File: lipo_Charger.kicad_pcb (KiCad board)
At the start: 4 copper layers, 99 parts, among them J1 XT60PW-M, J3 balance_plug_4s, J4 Conn_01x05, J5 Conn_01x04, J7 Conn_01x07, Q1 NX7002AK_215(nch low power), Q2 NVTFS010N10MCLTAG(high power), Q3 NVTFS010N10MCLTAG(high power), Q4 NVTFS010N10MCLTAG(high power), Q5 NVTFS010N10MCLTAG(high power)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

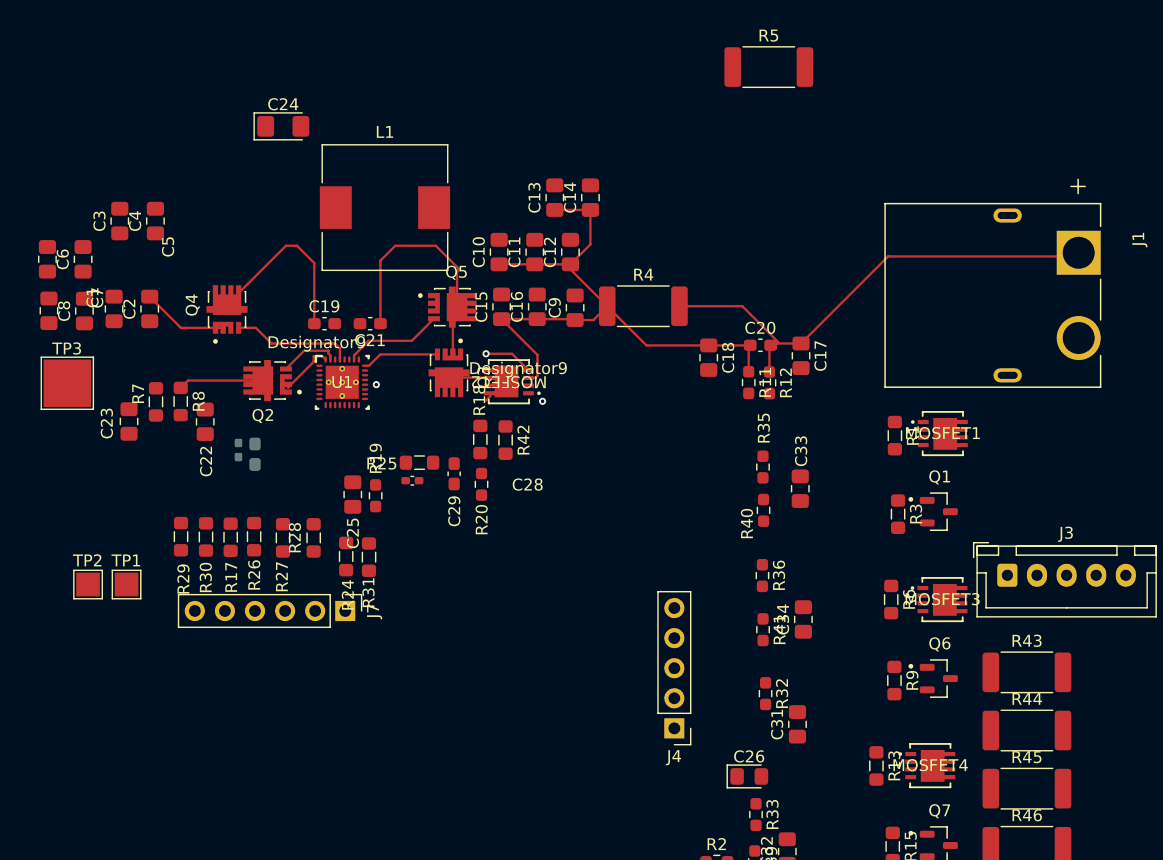
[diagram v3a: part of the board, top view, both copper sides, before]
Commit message: power side routing is done need to look into where i switch layers balancing side and interection with stm has to be done
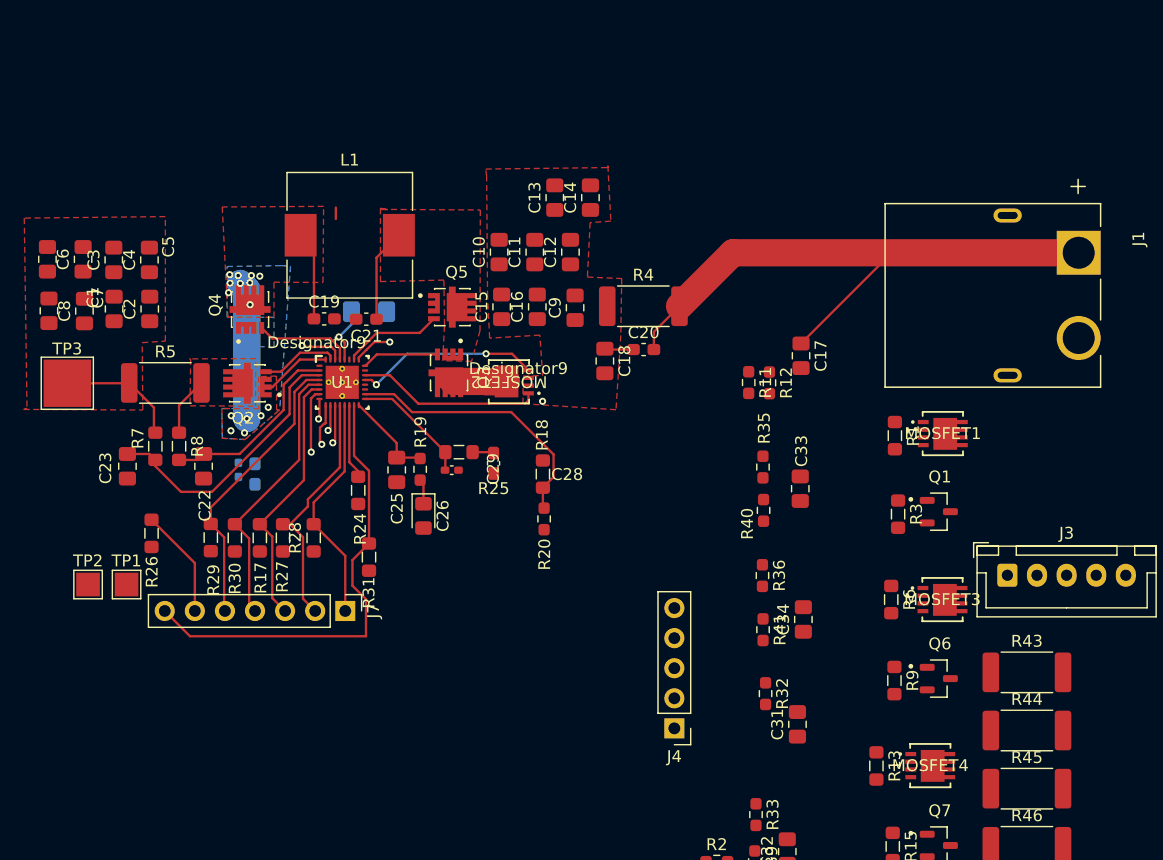
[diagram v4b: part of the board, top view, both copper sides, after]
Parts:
- removed R42: 10k, Inductor_SMD:L_0805_2012Metric_Pad1.05x1.20mm_HandSolder
- C24: moved to B.Cu
- J7: footprint Connector_PinHeader_2.54mm:PinHeader_1x06_P2.54mm_Vertical -> Connector_PinHeader_2.54mm:PinHeader_1x07_P2.54mm_Vertical
- moved R5 57.5 mm to (109.1, 72.7)
- moved C26 35.2 mm to (130.9, 83.9), turned to -90 degrees
- moved C24 17.2 mm to (126.3, 66.6)
- moved C20 9.87 mm to (149.5, 69.8)
- moved C18 8.77 mm to (146.2, 70.8)
- moved R26 8.67 mm to (107.9, 85.4)
- moved R18 6.04 mm to (141.0, 80.4)
- moved R20 6.04 mm to (141.1, 84.2)
- moved R24 5.68 mm to (125.4, 81.7)
- moved R19 4.37 mm to (130.6, 80.0)
- moved C25 4.25 mm to (128.6, 80.0)
- moved C23 3.78 mm to (105.9, 79.7)
- moved R8 3.78 mm to (110.3, 78.0)
- moved L1 3.78 mm to (124.7, 60.2)
- moved C22 3.75 mm to (112.3, 79.7)
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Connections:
- C19 pad 1: Net-(U1-SW1) -> /copper_pour2
- C21 pad 1: /copper_pour2 -> /copper_pour3
- J7 pad 1: /CMPOUT -> /SDA
- J7 pad 2: /ILIM_HIZ -> /SCL
- J7 pad 3: /CHRG_OK -> /ILIM_HIZ
- J7 pad 5: /PROCHOT_N -> /CHRG_OK
- J7 pad 6: /SDA -> /PROCHOT_N
- L1 pad 1: Net-(U1-SW1) -> /copper_pour2
- L1 pad 2: /copper_pour2 -> /copper_pour3
- MOSFET2 pad 5: /copper_pour3 -> Net-(MOSFET2-D-Pad5)
- Q2 pad 1-2-3: Net-(U1-SW1) -> /copper_pour2
- Q3 pad 1-2-3: /copper_pour2 -> /copper_pour3
- Q3 pad 5-6-7-8: /copper_pour3 -> Net-(MOSFET2-D-Pad5)
- Q4 pad 5-6-7-8: Net-(U1-SW1) -> /copper_pour2
- Q5 pad 5-6-7-8: /copper_pour2 -> /copper_pour3
- U1 pad 23: /copper_pour2 -> /copper_pour3
- U1 pad 32: Net-(U1-SW1) -> /copper_pour2
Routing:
- net /CMPOUT: track 0.00 -> 39.0 mm
- net /VSYS: track 51.2 -> 18.0 mm
- net /BAT: track 43.5 -> 68.4 mm
- net /CHRG_OK: track 0.00 -> 24.4 mm
- net /EN_OTG: track 0.00 -> 23.3 mm
- net Net-(U1-ACP): track 0.00 -> 23.2 mm
- net Net-(U1-CELL_BATPRES): track 0.00 -> 23.0 mm
- net /ILIM_HIZ: track 0.00 -> 22.1 mm
- net /SCL: track 0.00 -> 20.6 mm
- net Net-(U1-SW1): track 20.2 -> 0.00 mm
- net /SDA: track 0.00 -> 19.6 mm
- net Net-(U1-ACN): track 0.00 -> 16.2 mm
- net /PROCHOT_N: track 0.00 -> 12.5 mm, vias 0 -> 1
- net Net-(MOSFET2-G): track 4.16 -> 15.6 mm
- net +24V: track 0.00 -> 10.4 mm
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- added copper zone on B.Cu, net (none)
- added copper zone on F.Cu, net +24V
- added copper zone on F.Cu, net /VSYS
- added copper zone on F.Cu, net /copper_pour1
- added copper zone on F.Cu, net /copper_pour2
- added copper zone on F.Cu, net /copper_pour3
- added copper zone on In1.Cu, net GND

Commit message: done everything need to check before ordering once
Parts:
- added D1: LED, LED_THT:LED_D5.0mm, F.Cu at (127.6, 106.4)
- added D2: LED, LED_THT:LED_D5.0mm, F.Cu at (128.0, 113.0)
- added D3: LED, LED_THT:LED_D5.0mm, F.Cu at (128.5, 119.8)
- added D4: LED, LED_THT:LED_D5.0mm, F.Cu at (128.5, 126.5)
- added J2: Conn_01x01, Connector_PinHeader_2.54mm:PinHeader_1x01_P2.54mm_Vertical, F.Cu at (125.3, 97.2)
- added J6: Conn_01x01, Connector_PinHeader_2.54mm:PinHeader_1x01_P2.54mm_Vertical, F.Cu at (129.9, 97.2)
- added J8: Conn_01x04, Connector_PinHeader_2.54mm:PinHeader_1x04_P2.54mm_Vertical, F.Cu at (102.0, 112.9)
- added R10: 0ohm, Resistor_SMD:R_0603_1608Metric_Pad0.98x0.95mm_HandSolder, F.Cu at (130.6, 88.8)
- added R14: R, Resistor_THT:R_Axial_DIN0204_L3.6mm_D1.6mm_P5.08mm_Horizontal, F.Cu at (111.4, 110.5)
- added R22: R, Resistor_THT:R_Axial_DIN0204_L3.6mm_D1.6mm_P5.08mm_Horizontal, F.Cu at (111.4, 113.1)
- added R38: R, Resistor_THT:R_Axial_DIN0204_L3.6mm_D1.6mm_P5.08mm_Horizontal, F.Cu at (111.3, 116.6)
- added R42: R, Resistor_THT:R_Axial_DIN0204_L3.6mm_D1.6mm_P5.08mm_Horizontal, F.Cu at (110.9, 120.3)
- added TP4: TestPoint, TestPoint:TestPoint_THTPad_4.0x4.0mm_Drill2.0mm, F.Cu at (100.7, 79.4)
- TP3: footprint TestPoint:TestPoint_Pad_4.0x4.0mm -> TestPoint:TestPoint_THTPad_4.0x4.0mm_Drill2.0mm
- moved J5 37.6 mm to (148.8, 101.0), turned to 180 degrees
- moved R46 32.4 mm to (156.3, 131.8), turned to 180 degrees
- moved R45 25.8 mm to (159.6, 120.0)
- moved R43 25.7 mm to (157.5, 89.0), turned to -90 degrees
- moved Q8 23.4 mm to (151.1, 126.9)
- moved R21 23.4 mm to (147.2, 127.0)
- moved Q1 21.8 mm to (152.6, 84.6)
- moved R3 21.5 mm to (149.5, 85.1)
- moved Q7 21.0 mm to (153.5, 113.8)
- moved R15 21.0 mm to (149.6, 113.8)
- moved R44 19.7 mm to (162.3, 104.4), turned to -90 degrees
- moved MOSFET1 18.6 mm to (157.0, 82.5), turned to 180 degrees
- moved MOSFET4 18.5 mm to (158.1, 115.0), turned to 180 degrees
- moved MOSFET5 18.2 mm to (156.4, 126.9), turned to 180 degrees
- moved C34 18.2 mm to (144.8, 91.7)
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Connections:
- C24 pad 2: GNDA -> GND
- C30 pad 1: GND -> GNDA
- R37 pad 2: GND -> GNDA
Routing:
- net GNDA: track 0.00 -> 161.8 mm, vias 0 -> 6
- net /CELL_1S: track 0.00 -> 95.6 mm, vias 0 -> 1
- net /CELL_2S: track 0.00 -> 82.1 mm, vias 0 -> 1
- net GND: track 0.00 -> 80.3 mm, vias 0 -> 25
- net /CELL_3S: track 0.00 -> 48.5 mm
- net /CELL_4S: track 0.00 -> 43.6 mm
- net +24V: track 10.4 -> 53.5 mm, vias 0 -> 2
- net Net-(U1-PSYS): track 2.22 -> 34.6 mm, vias 1 -> 2
- net Net-(J5-Pin_1): track 0.00 -> 28.5 mm
- net Net-(U1-IBAT): track 3.61 -> 29.8 mm, vias 1 -> 2
- net Net-(U1-SRN): track 0.00 -> 25.9 mm
- net /CELL_1S_adc: track 0.00 -> 24.3 mm, vias 0 -> 1
- net Net-(U1-SRP): track 0.00 -> 24.0 mm
- net /BAT_adc: track 0.00 -> 19.4 mm
- net /PROCHOT_N: track 12.5 -> 31.5 mm, vias 1 -> 2
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- added copper zone on F.Cu, net GND
- added copper zone on In2.Cu, net VDDA
- removed copper zone on B.Cu, net (none)
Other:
- board outline added: 81.4 x 80.8 mm
- board text added: "3v3"

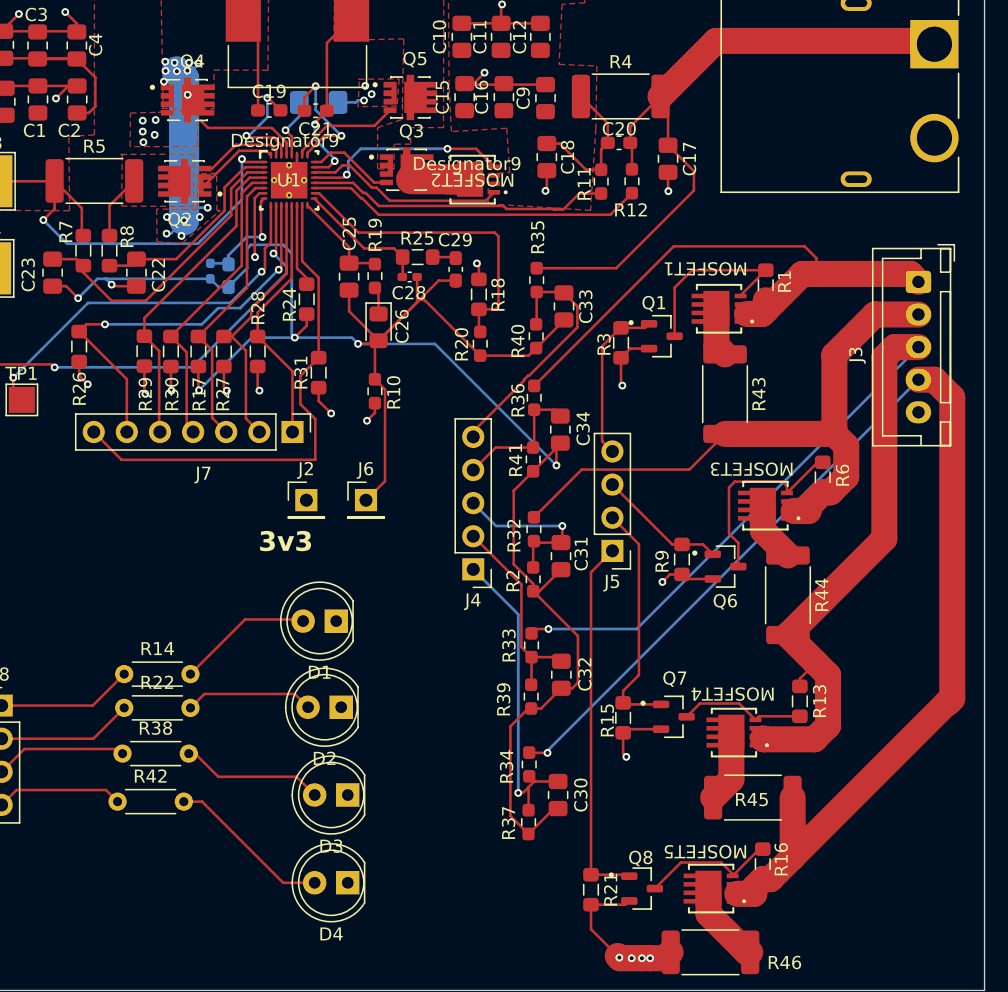
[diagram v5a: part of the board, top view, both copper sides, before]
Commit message: silk screen labelling done for headers
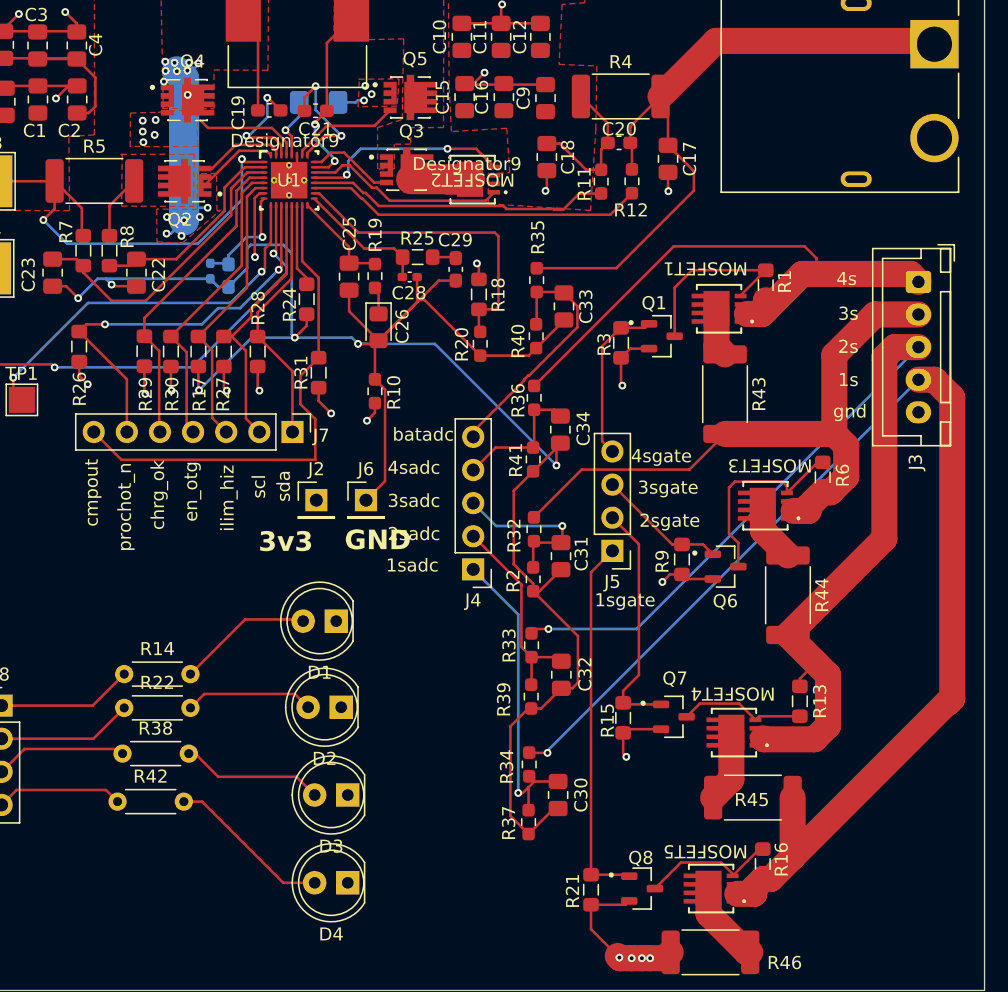
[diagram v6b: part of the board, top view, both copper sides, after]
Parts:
- moved J2 0.76 mm to (126.1, 97.2)
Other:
- board text added: "1s"
- board text added: "1sadc"
- board text added: "1sgate"
- board text added: "2s"
- board text added: "2sadc"
- board text added: "2sgate"
- board text added: "3s"
- board text added: "3sadc"
- board text added: "3sgate"
- board text added: "4s"
- board text added: "4sadc"
- board text added: "4sgate"
- board text added: "GND"
- board text added: "batadc"
- board text added: "chrg_ok"
- board text added: "cmpout"
- board text added: "en_otg"
- board text added: "gnd"
- board text added: "ilim_hiz"
- board text added: "prochot_n"
- board text added: "scl"
- board text added: "sda"
